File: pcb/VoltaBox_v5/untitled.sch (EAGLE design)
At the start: 63 parts, among them J1 0, X1 112J-TDAR-R(MICROSD), X2 52892-0895, X3 52892-0895, X4 XT30PW-F, X6 XT60PW-M, X7 KLS1-233

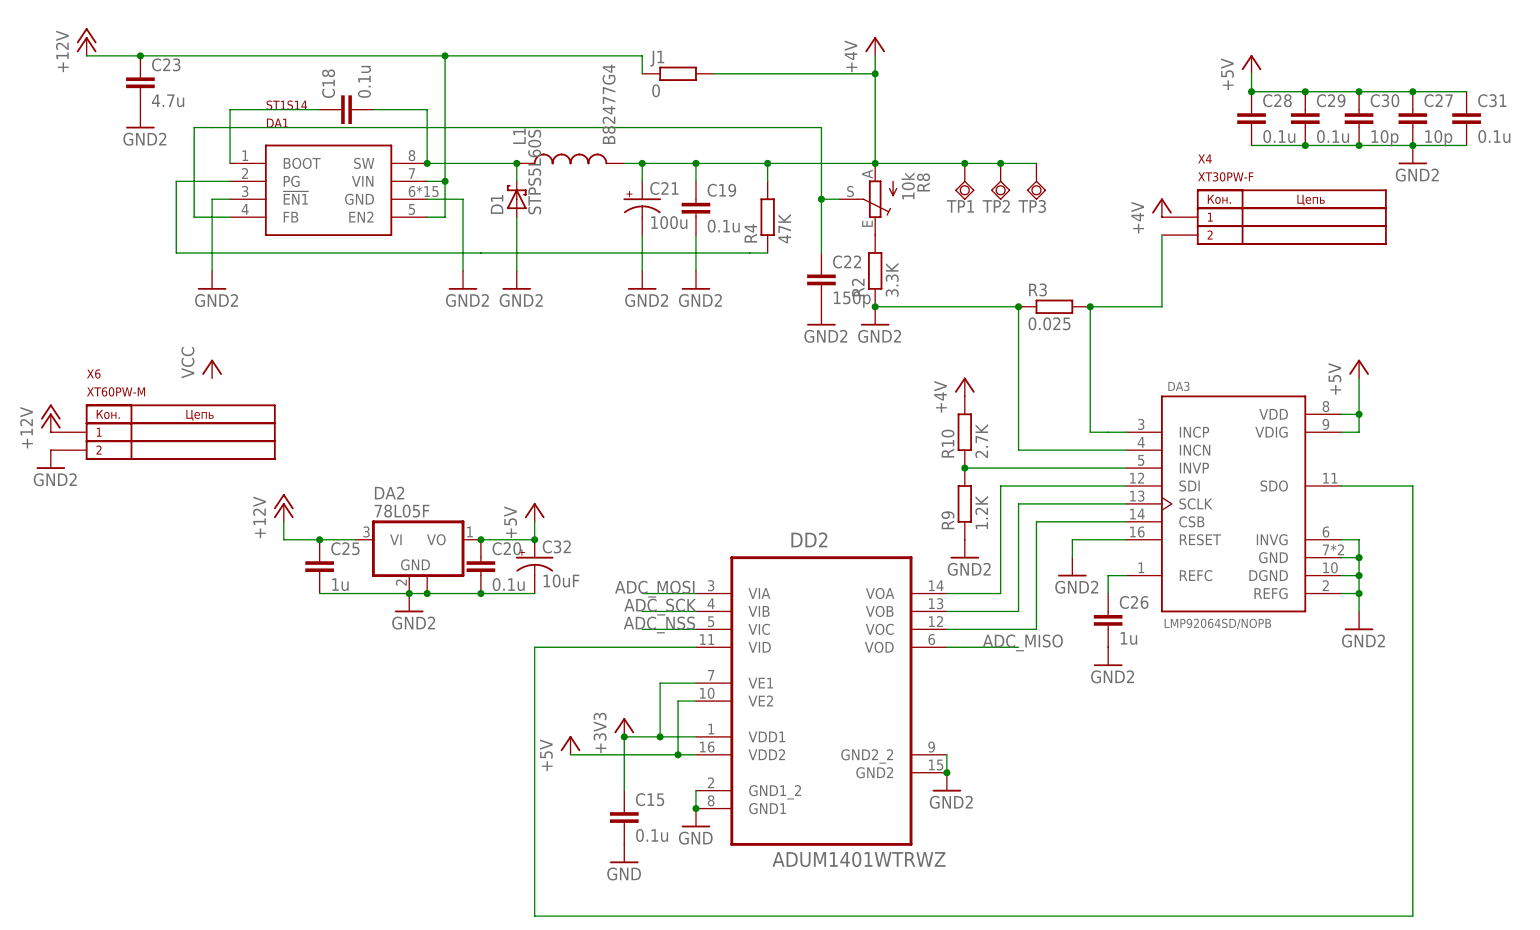
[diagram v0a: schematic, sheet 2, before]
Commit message: Changed all GND nets in dc-dc and adc part to AGND. Changed usb footprint to correct usb footprint (kls1-233-1-x-x to kls1-233-0-x-x (it's doesn't need holes in pcb that must be very close to the connector's pads)). X2 shifted down. Added some via in dc-dc.
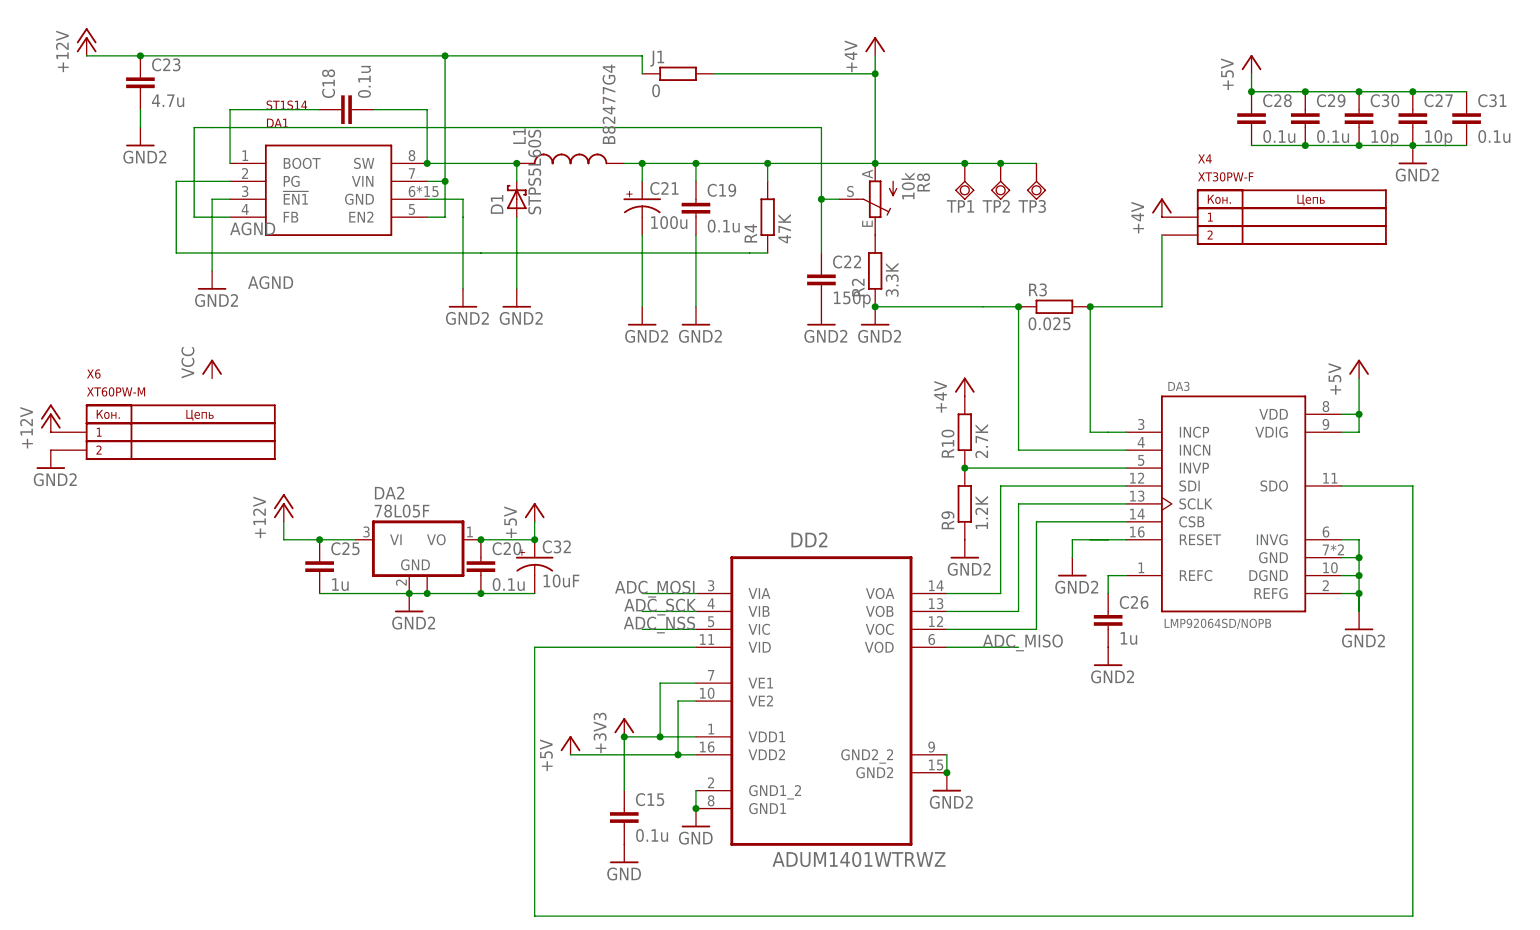
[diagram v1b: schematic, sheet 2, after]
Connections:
- new net AGND: C19.2, C20.2, C21.-, C22.2, C23.2, C25.2, C26.2, C27.2, C28.2, C29.2, C30.2, C31.2, C32.-, D1.A, DA1.!EN1, DA1.GND, DA2.GND, DA2.GND@1, DA3.DGND, DA3.GND, DA3.INCN, DA3.INVG, DA3.REFG, DA3.RESET, DD2.GND2, DD2.GND2_2, R2.1, R3.1, R9.1, X6.P$2
- net GND: no longer C19.2, C20.2, C21.-, C22.2, C23.2, C25.2, C26.2, C27.2, C28.2, C29.2, C30.2, C31.2, C32.-, D1.A, DA1.!EN1, DA1.GND, DA2.GND, DA2.GND@1, DA3.DGND, DA3.GND, DA3.INCN, DA3.INVG, DA3.REFG, DA3.RESET, DD2.GND2, DD2.GND2_2, R2.1, R3.1, R9.1, X6.P$2

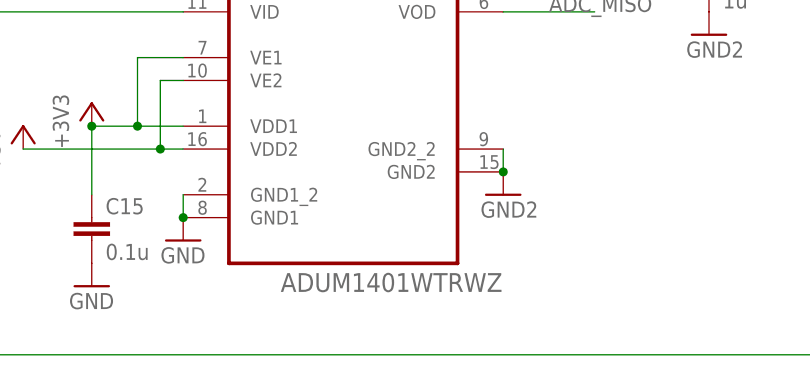
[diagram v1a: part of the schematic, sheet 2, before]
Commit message: Relocated all silk labels to it's places. Renamed isolator's model. Added some text to the top silk (tPlace).
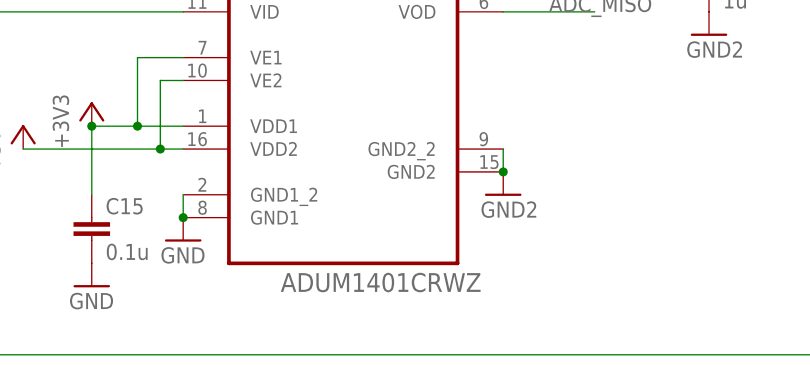
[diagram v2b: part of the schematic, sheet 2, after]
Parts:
- DD2: value ADUM1401WTRWZ -> ADUM1401CRWZ; device ADUM1401WTRWZ:ADUM1401WTRWZ -> ADUM1401WTRWZ:ADUM1401CRWZ
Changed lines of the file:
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@@
 <part name="GND10" library="supply1" library_urn="urn:adsk.eagle:library:371" deviceset="GND" device=""/>
 <part name="C16" library="eagle-ltspice" library_urn="urn:adsk.eagle:library:217" deviceset="C" device="C0603" package3d_urn="urn:adsk.eagle:package:13262/1" value="15p"/>
-<part name="C17" library="eagle-ltspice" library_urn="urn:adsk.eagle:library:217" deviceset="C" device="C0603" package3d_urn="urn:adsk.eagle:package:13262/1" value="15p"/>
 <part name="GND11" library="supply1" library_urn="urn:adsk.eagle:library:371" deviceset="GND" device=""/>
 <part name="GND12" library="supply1" library_urn="urn:adsk.eagle:library:371" deviceset="GND" device=""/>
@@
 <part name="P+8" library="supply1" library_urn="urn:adsk.eagle:library:371" deviceset="+5V" device=""/>
 <part name="P+9" library="supply1" library_urn="urn:adsk.eagle:library:371" deviceset="+5V" device=""/>
-<part name="DD2" library="ADUM1401WTRWZ" deviceset="ADUM1401WTRWZ" device=""/>
+<part name="DD2" library="ADUM1401WTRWZ" deviceset="ADUM1401CRWZ" device=""/>
 <part name="C26" library="eagle-ltspice" library_urn="urn:adsk.eagle:library:217" deviceset="C" device="C0603" package3d_urn="urn:adsk.eagle:package:13262/1" value="1u"/>
 <part name="U$14" library="untitled" deviceset="GND2" device=""/>
@@
 <part name="U$3" library="untitled" deviceset="GND2" device=""/>
 <part name="U$9" library="untitled" deviceset="GND2" device=""/>
+<part name="C17" library="eagle-ltspice" library_urn="urn:adsk.eagle:library:217" deviceset="C" device="C0603" package3d_urn="urn:adsk.eagle:package:13262/1" value="15p"/>
 </parts>
 <sheets>
@@
 <instance part="GND10" gate="1" x="132.08" y="99.06"/>
 <instance part="C16" gate="G$1" x="-25.4" y="63.5"/>
-<instance part="C17" gate="G$1" x="-10.16" y="63.5"/>
 <instance part="GND11" gate="1" x="-25.4" y="55.88"/>
 <instance part="GND12" gate="1" x="-10.16" y="55.88"/>
@@
 <instance part="GND14" gate="1" x="33.02" y="124.46"/>
 <instance part="X7" gate="G$1" x="165.1" y="78.74"/>
+<instance part="C17" gate="G$1" x="-10.16" y="63.5"/>
 </instances>
 <busses>
@@
 </segment>
 <segment>
-<pinref part="C17" gate="G$1" pin="2"/>
-<pinref part="GND12" gate="1" pin="GND"/>
-</segment>
-<segment>
 <pinref part="DD1" gate="G$1" pin="VSS_3"/>
 <wire x1="43.18" y1="101.6" x2="43.18" y2="104.14" width="0.1524" layer="91"/>
@@
 <pinref part="GND14" gate="1" pin="GND"/>
 <label x="35.56" y="127" size="1.778" layer="95"/>
+</segment>
+<segment>
+<pinref part="C17" gate="G$1" pin="2"/>
+<pinref part="GND12" gate="1" pin="GND"/>
 </segment>
 </net>
@@
 <pinref part="DD1" gate="G$1" pin="PC15-OSC32_OUT"/>
 <wire x1="-10.16" y1="78.74" x2="25.4" y2="78.74" width="0.1524" layer="91"/>
-<pinref part="C17" gate="G$1" pin="1"/>
 <wire x1="-10.16" y1="68.58" x2="-10.16" y2="66.04" width="0.1524" layer="91"/>
 <junction x="-10.16" y="68.58"/>
 <pinref part="ZQ1" gate="G$1" pin="2"/>
-</segment>
-</net>
+<pinref part="C17" gate="G$1" pin="1"/>
+</segment>
+</net>

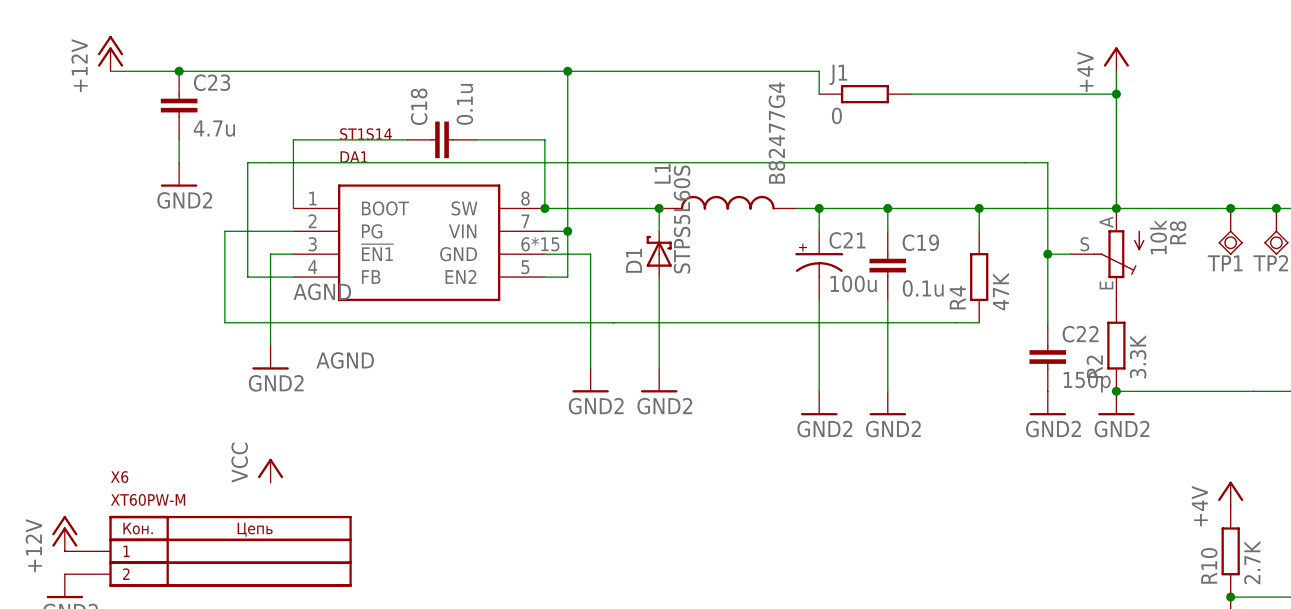
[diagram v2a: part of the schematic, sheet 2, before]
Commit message: VB5 DC-DC GND fixed, STM32 boot pin connected
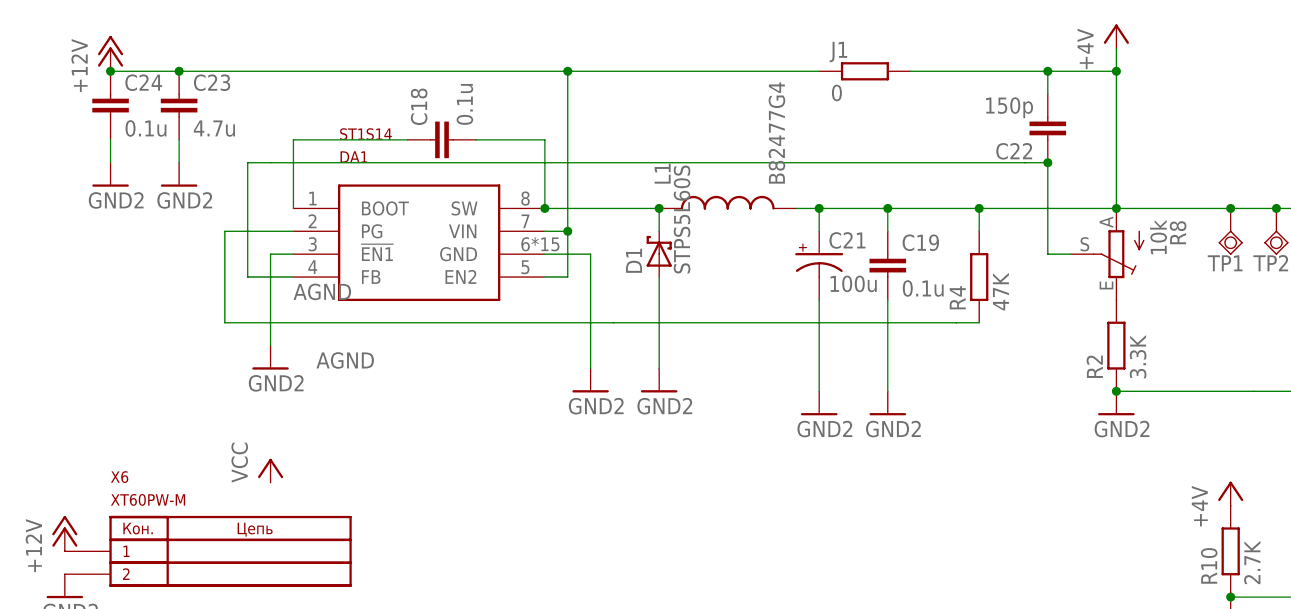
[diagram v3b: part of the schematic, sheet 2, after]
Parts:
- added C24: 0.1u, eagle-ltspice:CC0603
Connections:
- net +12V: now also C24.1
- net +4V: now also C22.2
- net AGND: now also C24.2; no longer C22.2
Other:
- moved on the sheet: C22, J1
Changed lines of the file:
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@@
 <part name="C20" library="eagle-ltspice" library_urn="urn:adsk.eagle:library:217" deviceset="C" device="C0603" package3d_urn="urn:adsk.eagle:package:13262/1" value="0.1u"/>
 <part name="C22" library="eagle-ltspice" library_urn="urn:adsk.eagle:library:217" deviceset="C" device="C0603" package3d_urn="urn:adsk.eagle:package:13262/1" value="150p"/>
-<part name="U$1" library="untitled" deviceset="GND2" device=""/>
 <part name="U$2" library="untitled" deviceset="GND2" device=""/>
 <part name="U$4" library="untitled" deviceset="GND2" device=""/>
@@
 <part name="U$9" library="untitled" deviceset="GND2" device=""/>
 <part name="C17" library="eagle-ltspice" library_urn="urn:adsk.eagle:library:217" deviceset="C" device="C0603" package3d_urn="urn:adsk.eagle:package:13262/1" value="15p"/>
+<part name="C24" library="eagle-ltspice" library_urn="urn:adsk.eagle:library:217" deviceset="C" device="C0603" package3d_urn="urn:adsk.eagle:package:13262/1" value="0.1u"/>
+<part name="U$20" library="untitled" deviceset="GND2" device=""/>
 </parts>
 <sheets>
@@
 <instance part="C19" gate="G$1" x="76.2" y="25.4"/>
 <instance part="C20" gate="G$1" x="45.72" y="-25.4"/>
-<instance part="C22" gate="G$1" x="93.98" y="15.24"/>
-<instance part="U$1" gate="G$1" x="93.98" y="7.62"/>
+<instance part="C22" gate="G$1" x="93.98" y="38.1" rot="R180"/>
 <instance part="U$2" gate="G$1" x="101.6" y="7.62"/>
 <instance part="U$4" gate="G$1" x="76.2" y="7.62"/>
@@
 <instance part="DA3" gate="G$1" x="152.4" y="-17.78"/>
 <instance part="R3" gate="G$1" x="127" y="10.16"/>
-<instance part="U$12" gate="G$1" x="101.6" y="48.26"/>
+<instance part="U$12" gate="G$1" x="101.6" y="50.8"/>
 <instance part="U$11" gate="G$1" x="170.18" y="-35.56"/>
 <instance part="DA2" gate="G$1" x="35.56" y="-22.86"/>
@@
 <instance part="X4" gate="G$1" x="142.24" y="22.86"/>
 <instance part="U$6" gate="G$1" x="142.24" y="25.4"/>
-<instance part="J1" gate="G$1" x="73.66" y="43.18"/>
+<instance part="J1" gate="G$1" x="73.66" y="45.72"/>
 <instance part="TP1" gate="G$1" x="114.3" y="27.94"/>
 <instance part="TP2" gate="G$1" x="119.38" y="27.94"/>
@@
 <instance part="U$3" gate="G$1" x="43.18" y="10.16"/>
 <instance part="U$9" gate="G$1" x="50.8" y="10.16"/>
+<instance part="C24" gate="G$1" x="-10.16" y="43.18"/>
+<instance part="U$20" gate="G$1" x="-10.16" y="33.02"/>
 </instances>
 <busses>
@@
 <wire x1="5.08" y1="22.86" x2="10.16" y2="22.86" width="0.1524" layer="91"/>
 <wire x1="91.44" y1="35.56" x2="93.98" y2="35.56" width="0.1524" layer="91"/>
-<pinref part="C22" gate="G$1" pin="1"/>
-<wire x1="93.98" y1="25.4" x2="93.98" y2="17.78" width="0.1524" layer="91"/>
 <pinref part="R8" gate="1" pin="S"/>
 <wire x1="93.98" y1="25.4" x2="96.52" y2="25.4" width="0.1524" layer="91"/>
 <wire x1="93.98" y1="35.56" x2="93.98" y2="25.4" width="0.1524" layer="91"/>
-<junction x="93.98" y="25.4"/>
 <pinref part="DA1" gate="G$1" pin="FB"/>
+<pinref part="C22" gate="G$1" pin="1"/>
+<junction x="93.98" y="35.56"/>
 </segment>
 </net>
@@
 <pinref part="J1" gate="G$1" pin="1"/>
 <wire x1="40.64" y1="45.72" x2="68.58" y2="45.72" width="0.1524" layer="91"/>
-<wire x1="68.58" y1="45.72" x2="68.58" y2="43.18" width="0.1524" layer="91"/>
 <junction x="40.64" y="45.72"/>
+<pinref part="C24" gate="G$1" pin="1"/>
+<junction x="-10.16" y="45.72"/>
 </segment>
 <segment>
@@
 <junction x="86.36" y="30.48"/>
 <pinref part="U$12" gate="G$1" pin="+4V"/>
-<wire x1="101.6" y1="30.48" x2="101.6" y2="43.18" width="0.1524" layer="91"/>
+<wire x1="101.6" y1="30.48" x2="101.6" y2="45.72" width="0.1524" layer="91"/>
 <junction x="101.6" y="30.48"/>
 <pinref part="L1" gate="G$1" pin="2"/>
 <pinref part="C21" gate="G$1" pin="+"/>
 <pinref part="J1" gate="G$1" pin="2"/>
-<wire x1="101.6" y1="43.18" x2="101.6" y2="45.72" width="0.1524" layer="91"/>
-<wire x1="78.74" y1="43.18" x2="101.6" y2="43.18" width="0.1524" layer="91"/>
-<junction x="101.6" y="43.18"/>
+<wire x1="101.6" y1="45.72" x2="101.6" y2="48.26" width="0.1524" layer="91"/>
+<wire x1="78.74" y1="45.72" x2="93.98" y2="45.72" width="0.1524" layer="91"/>
+<junction x="101.6" y="45.72"/>
 <pinref part="TP1" gate="G$1" pin="TP"/>
+<wire x1="93.98" y1="45.72" x2="101.6" y2="45.72" width="0.1524" layer="91"/>
 <wire x1="101.6" y1="30.48" x2="114.3" y2="30.48" width="0.1524" layer="91"/>
 <pinref part="TP2" gate="G$1" pin="TP"/>
@@
 <wire x1="124.46" y1="30.48" x2="119.38" y2="30.48" width="0.1524" layer="91"/>
 <junction x="119.38" y="30.48"/>
+<pinref part="C22" gate="G$1" pin="2"/>
+<wire x1="93.98" y1="43.18" x2="93.98" y2="45.72" width="0.1524" layer="91"/>
+<junction x="93.98" y="45.72"/>
 </segment>
 <segment>
@@
 <pinref part="U$18" gate="G$1" pin="AGND"/>
 <pinref part="R9" gate="G$1" pin="1"/>
-</segment>
-<segment>
-<pinref part="C22" gate="G$1" pin="2"/>
-<pinref part="U$1" gate="G$1" pin="AGND"/>
 </segment>
 <segment>
@@
 <wire x1="170.18" y1="-33.02" x2="170.18" y2="-30.48" width="0.1524" layer="91"/>
 </segment>
-</net>
+<segment>
+<pinref part="U$20" gate="G$1" pin="AGND"/>
+<pinref part="C24" gate="G$1" pin="2"/>
+<wire x1="-10.16" y1="35.56" x2="-10.16" y2="38.1" width="0.1524" layer="91"/>
+</segment>
+</net>
